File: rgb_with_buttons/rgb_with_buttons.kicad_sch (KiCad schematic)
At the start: 22 parts, among them J1 ISP, J4 Barrel_Jack_Switch, SW1 SW_MEC_5E, SW2 SW_MEC_5E, SW3 SW_MEC_5E, U1 ATmega328P-P, Y1 Crystal

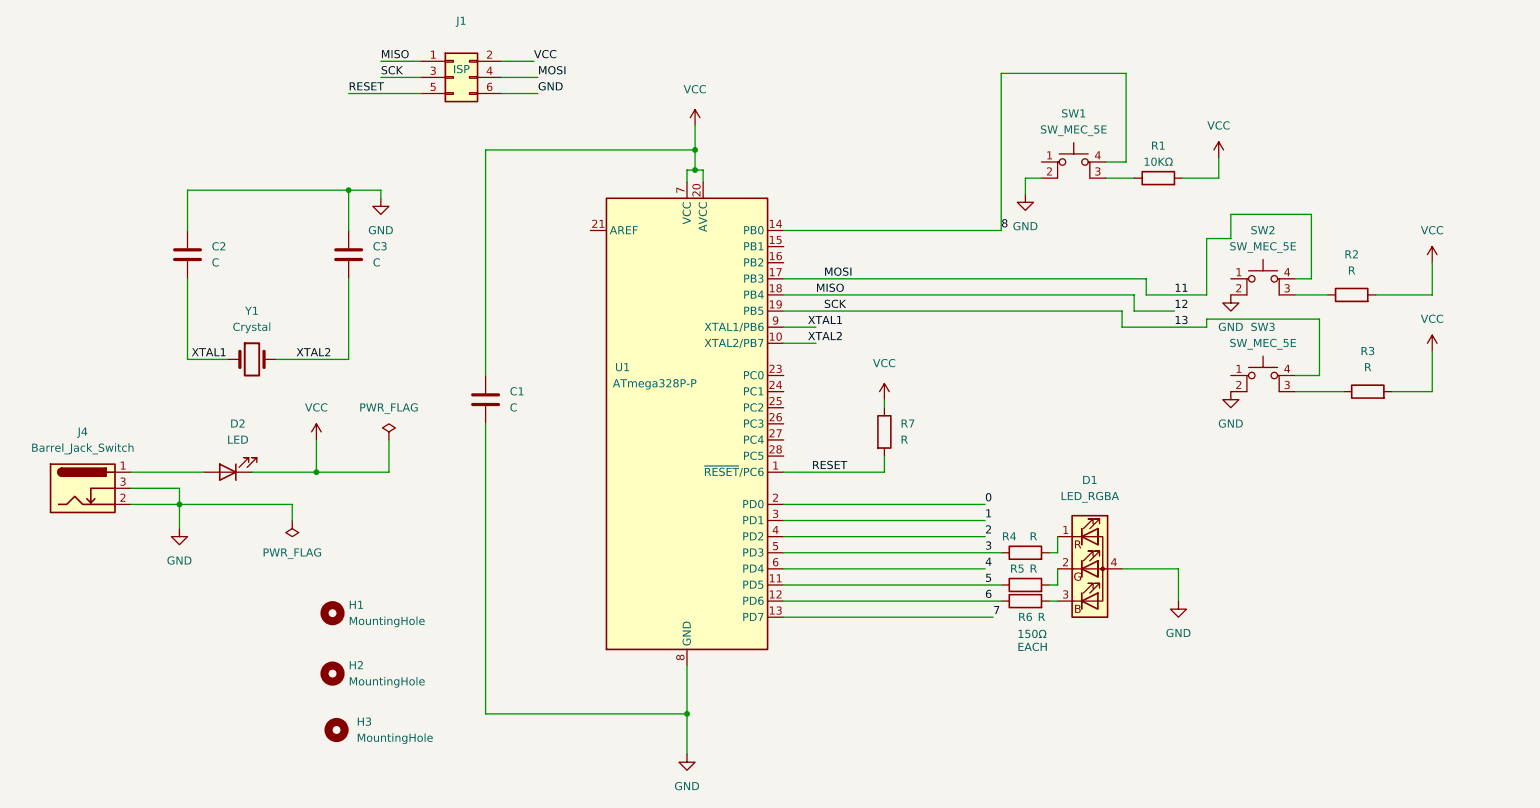
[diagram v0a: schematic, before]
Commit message: all pcb is ready, not quite beautiful but functioning
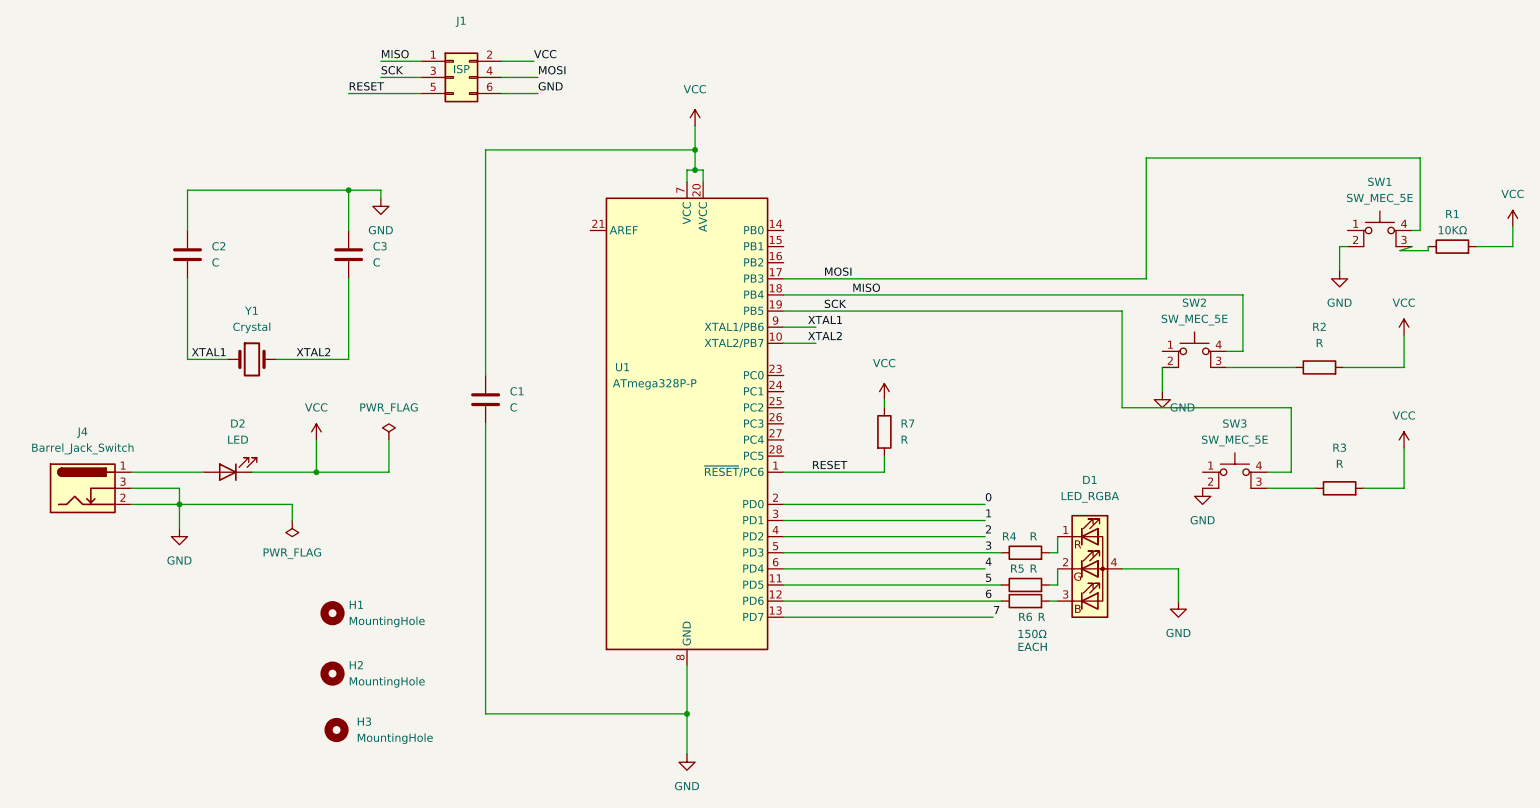
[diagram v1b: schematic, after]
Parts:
- H1, H2, H3: footprint (none) -> MountingHole:MountingHole_3.2mm_M3
- J1: footprint (none) -> Connector_PinHeader_2.54mm:PinHeader_2x03_P2.54mm_Vertical
- Y1: footprint (none) -> Crystal:Crystal_HC49-4H_Vertical
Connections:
- net 11 renamed MOSI
- net MOSI: now also SW1.4 (A); no longer SW2.4 (A)
- net 12 renamed MISO
- net MISO: now also SW2.4 (A)
- net 13 renamed SCK
- net 8: no longer names the net of U1.14 (PB0)
- net 8: no longer SW1.4 (A)
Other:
- moved on the sheet: R1, R2, R3, SW1, SW2, SW3

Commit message: pcb is now complete(only warnings in DRC due to problem of the led design), had to change the symbol of the button a bit(nothing significant pin numbers only)
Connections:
- net MISO: now also SW2.1 (b2); no longer SW2.4 (A)
- net MOSI: now also SW1.1 (b2); no longer SW1.4 (A)
- net SCK: now also SW3.1 (b2); no longer SW3.4 (A)
- net at R1.1: now also SW1.1 (b2); no longer SW1.3 (K)
- net at R3.1: now also SW3.1 (b2); no longer SW3.3 (K)
- net at R2.1: now also SW2.1 (b2); no longer SW2.3 (K)
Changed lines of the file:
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@@
     (stroke (width 0) (type default) (color 0 0 0 0))
   )
-  (wire (pts (xy 240.665 78.105) (xy 245.11 78.105))
+  (wire (pts (xy 240.665 83.82) (xy 245.11 81.28))
     (stroke (width 0) (type default) (color 0 0 0 0))
   )
@@
     (stroke (width 0) (type default) (color 0 0 0 0))
   )
+  (wire (pts (xy 242.57 80.01) (xy 242.57 77.47))
+    (stroke (width 0) (type default) (color 0 0 0 0))
+  )
   (wire (pts (xy 186.69 125.73) (xy 186.69 123.19))
     (stroke (width 0) (type default) (color 0 0 0 0))
@@
     (stroke (width 0) (type default) (color 0 0 0 0))
   )
-  (wire (pts (xy 240.665 78.105) (xy 242.57 77.47))
+  (wire (pts (xy 240.665 83.82) (xy 242.57 80.01))
     (stroke (width 0) (type default) (color 0 0 0 0))
   )
@@
     (stroke (width 0) (type default) (color 0 0 0 0))
   )
-  (wire (pts (xy 245.11 78.105) (xy 245.11 77.47))
+  (wire (pts (xy 245.11 81.28) (xy 245.11 77.47))
     (stroke (width 0) (type default) (color 0 0 0 0))
   )
@@
     (pin "2")
   )
-  (symbol (lib_id "Switch:SW_MEC_5E") (at 237.49 77.47 0) (unit 1)
+  (symbol (lib_name "SW_MEC_5E_1") (lib_id "Switch:SW_MEC_5E") (at 237.49 77.47 0) (unit 1)
     (in_bom yes) (on_board yes) (fields_autoplaced)
     (property "Reference" "SW1" (id 0) (at 237.49 67.31 0))
@@
     )
     (pin "1")
-    (pin "2")
-    (pin "3")
-    (pin "4")
+    (pin "1")
+    (pin "2")
+    (pin "2")
   )
   (symbol (lib_id "Device:Crystal") (at 59.69 95.25 0) (unit 1)
@@
       (effects (font (size 1.27 1.27)) hide)
     )
-    (pin "1")
-    (pin "2")
-    (pin "3")
-    (pin "4")
-  )
-  (symbol (lib_id "Switch:SW_MEC_5E") (at 208.28 96.52 0) (unit 1)
+    (pin "2")
+    (pin "2")
+    (pin "1")
+    (pin "1")
+  )
+  (symbol (lib_name "SW_MEC_5E_2") (lib_id "Switch:SW_MEC_5E") (at 208.28 96.52 0) (unit 1)
     (in_bom yes) (on_board yes)
     (property "Reference" "SW2" (id 0) (at 208.28 86.36 0))
@@
     )
     (pin "1")
-    (pin "2")
-    (pin "3")
-    (pin "4")
+    (pin "1")
+    (pin "2")
+    (pin "2")
   )
   (symbol (lib_id "power:GND") (at 209.55 115.57 0) (unit 1)
